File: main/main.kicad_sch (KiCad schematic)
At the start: 0 parts

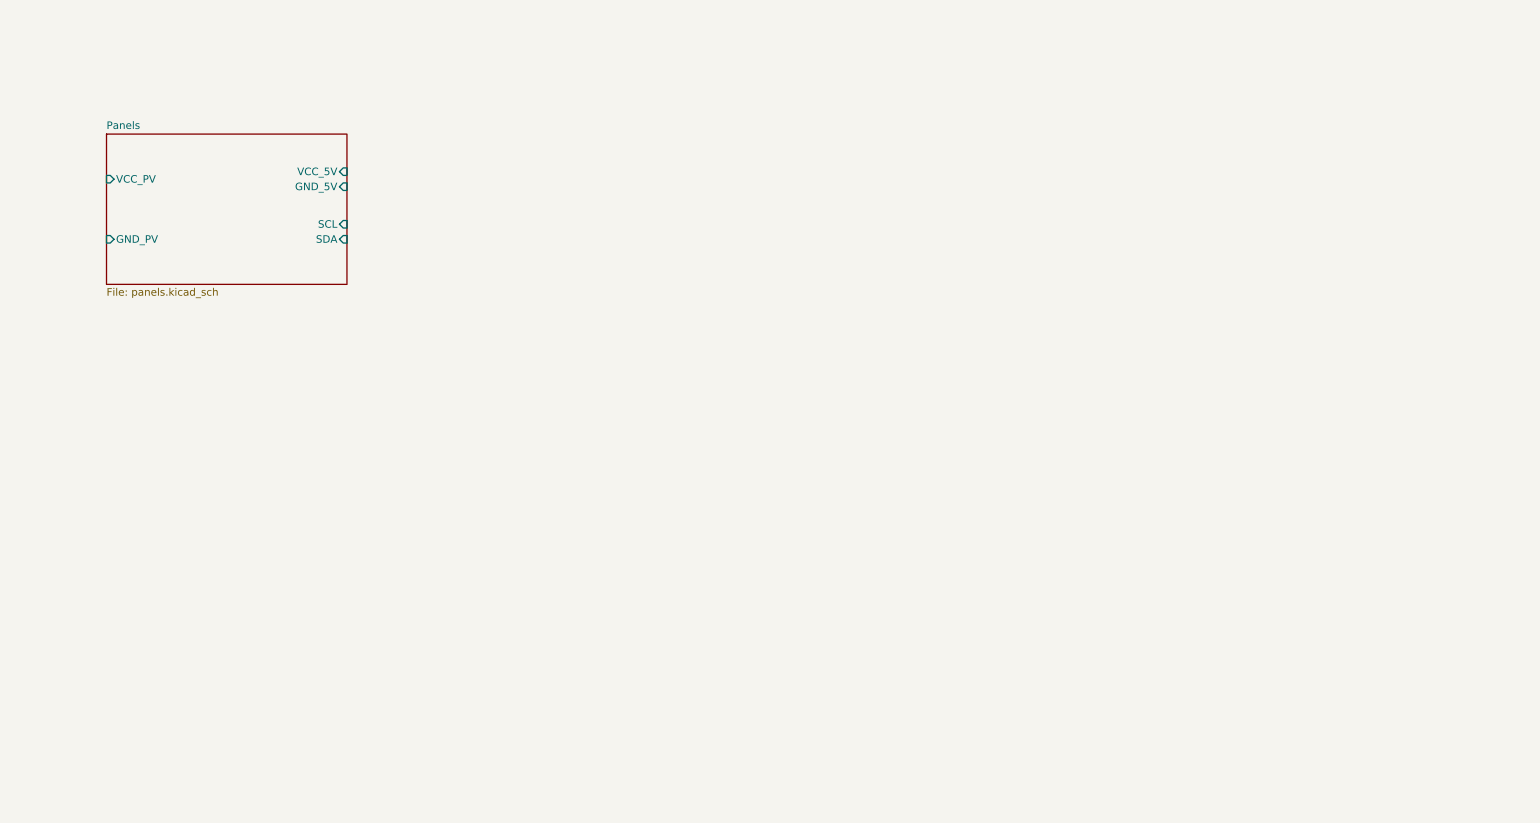
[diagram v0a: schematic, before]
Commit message: added MCU to PV
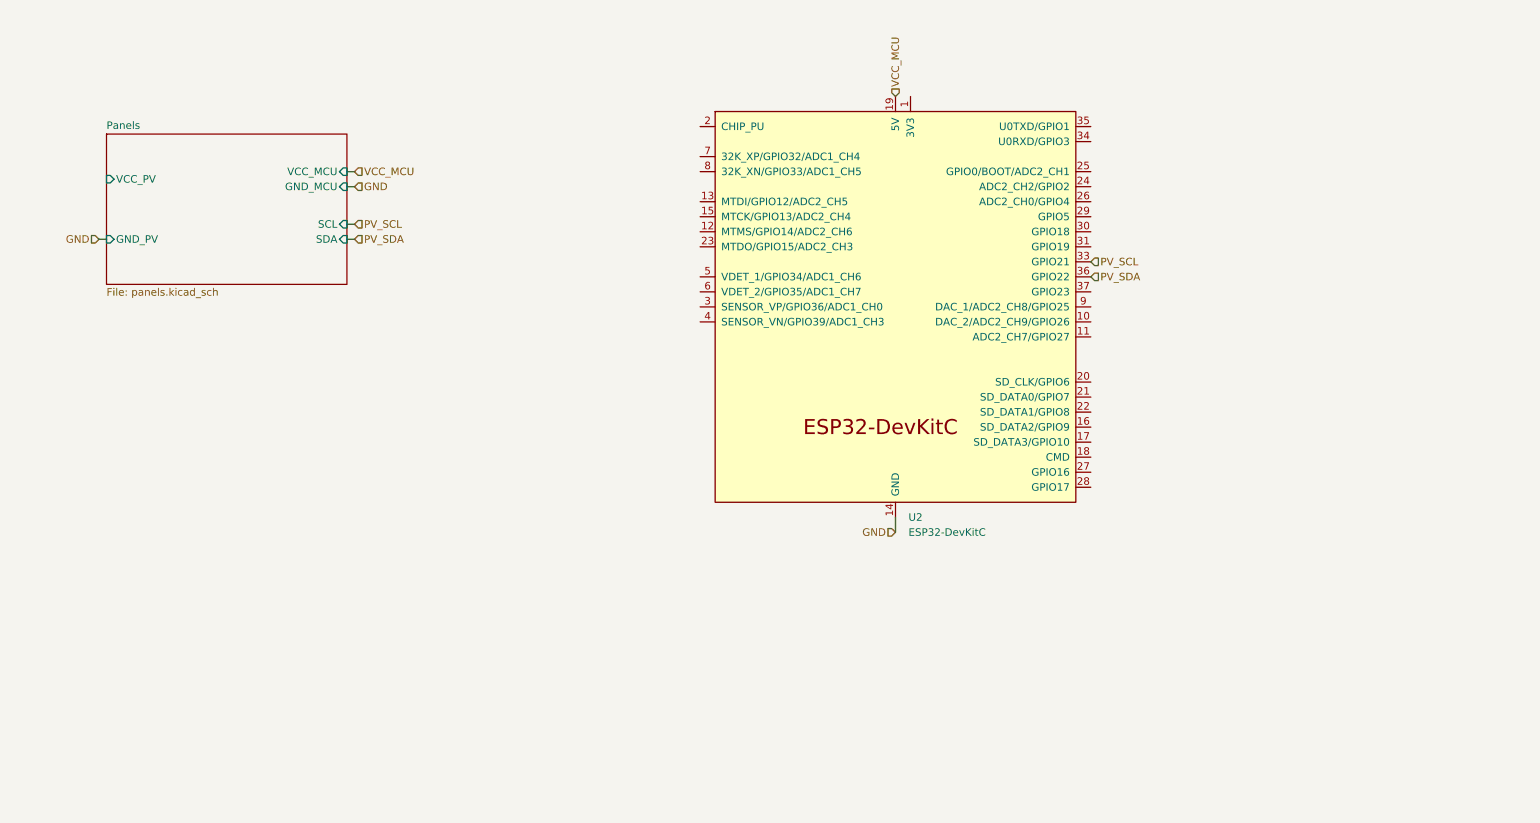
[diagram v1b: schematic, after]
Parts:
- added U2: ESP32-DevKitC, PCM_Espressif:ESP32-DevKitC, symbol PCM_Espressif:ESP32-DevKitC
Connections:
- new net GND: U2.14 (GND), U2.32 (GND), U2.38 (GND)
- new net PV_SCL: U2.33 (GPIO21)
- new net PV_SDA: U2.36 (GPIO22)
- new net VCC_MCU: U2.19 (5V)
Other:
- sheet Panels ports: added GND_MCU, VCC_MCU; removed GND_5V, VCC_5V

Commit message: added MPPT and Battery
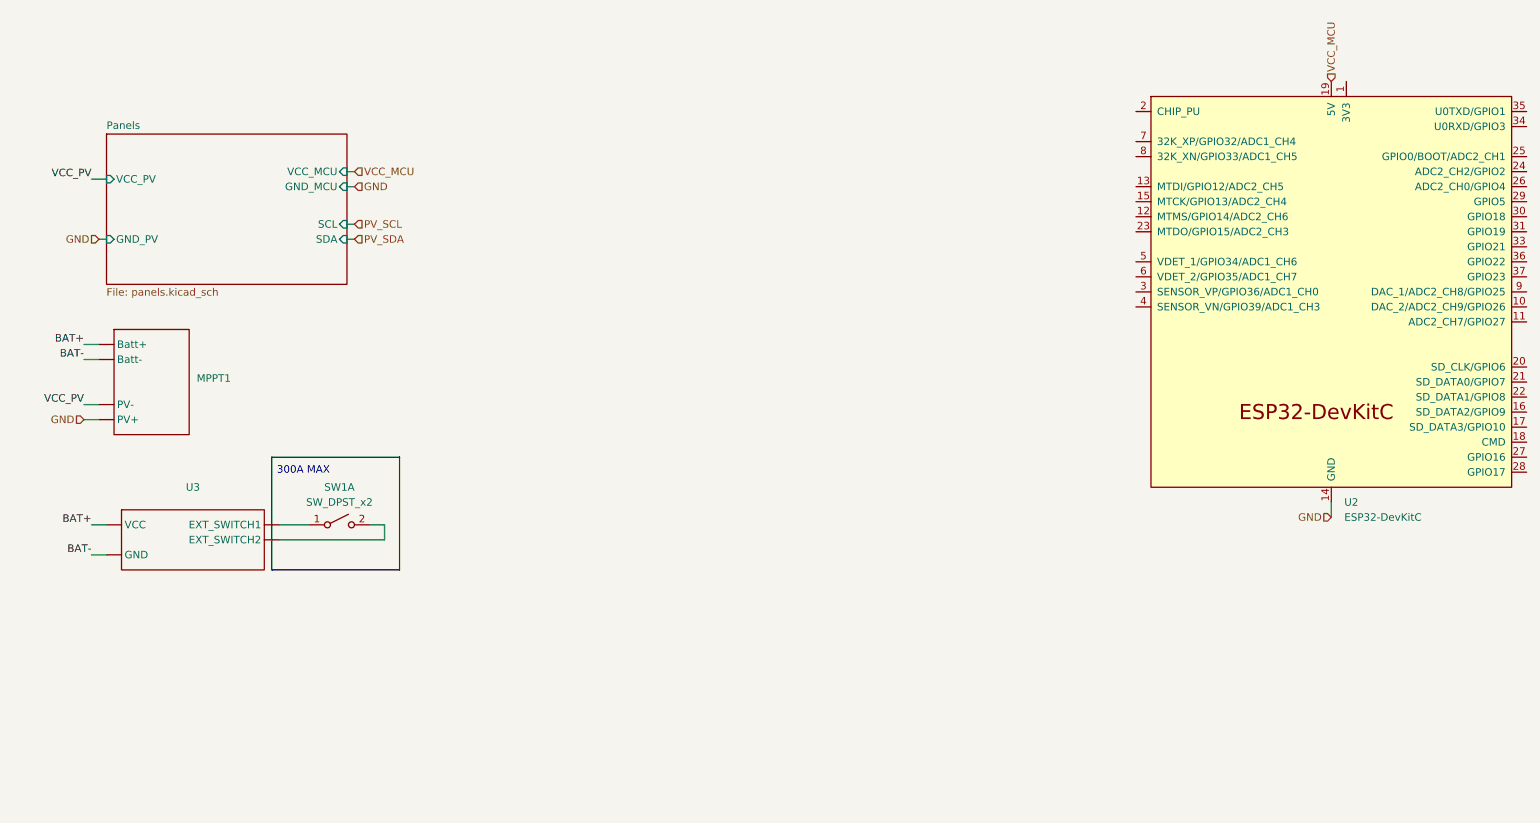
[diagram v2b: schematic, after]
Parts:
- added MPPT1: ~, symbol New_Library_0:MPPT_Victron_150{backslash}35
- added SW1: SW_DPST_x2, symbol Switch:SW_DPST_x2
- added U3: ~, symbol New_Library_0:Accumulator
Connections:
- net GND: now also MPPT1. (PV-)
- net PV_SCL: no longer U2.33 (GPIO21)
- net PV_SDA: no longer U2.36 (GPIO22)
- new net: SW1.1 (A), U3. (VCC)
- new net: SW1.2 (B), U3. (VCC)
- new net BAT+: MPPT1. (PV-), U3. (VCC)
- new net BAT-: MPPT1. (PV-), U3. (VCC)
- new net VCC_PV: MPPT1. (PV-)
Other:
- note added: "300A MAX"
- moved on the sheet: U2

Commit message: Added Central Control Unit Added Jetson Orin Nano
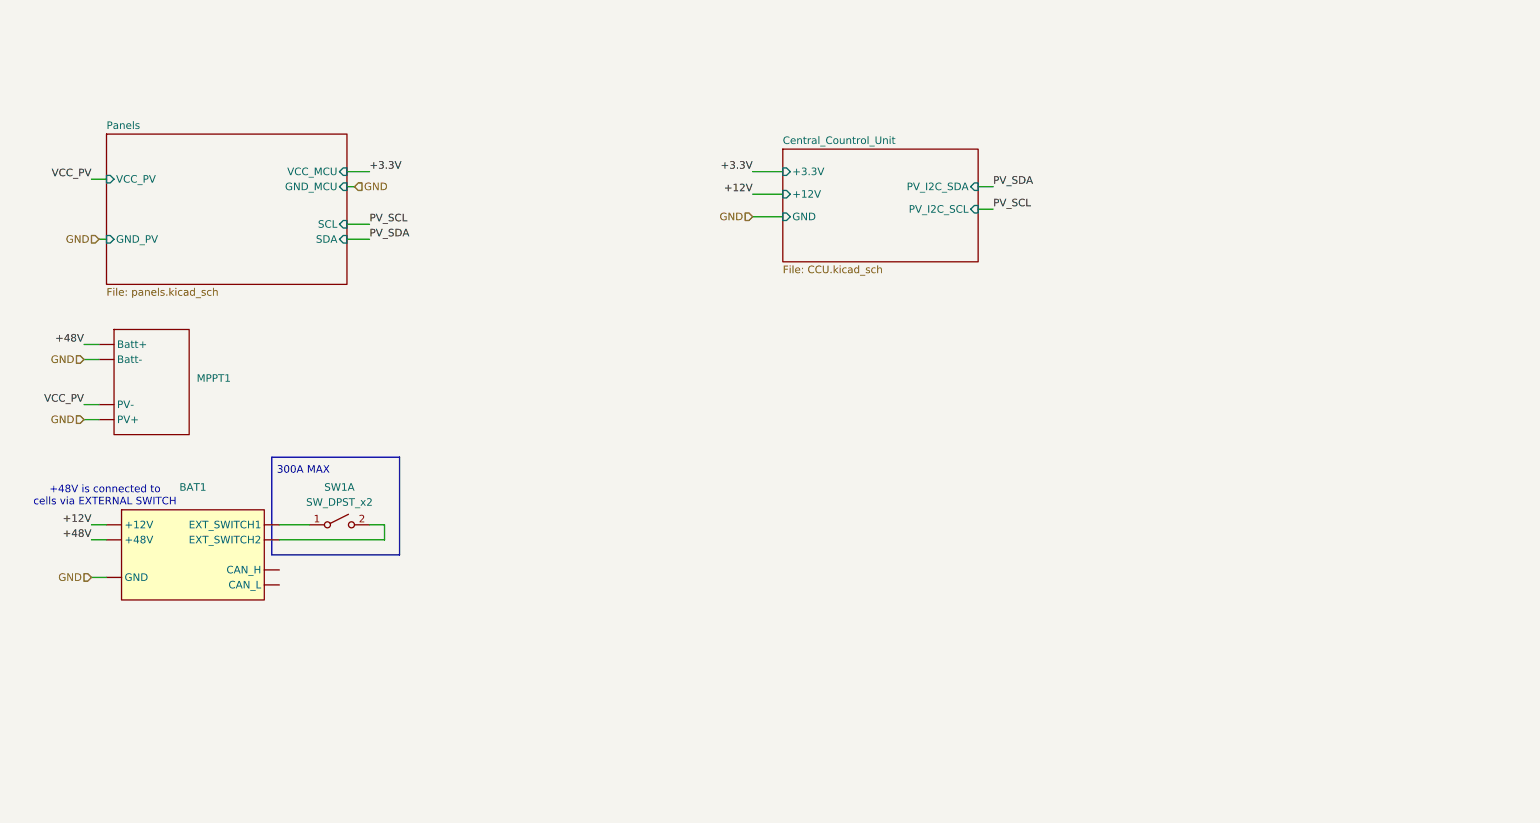
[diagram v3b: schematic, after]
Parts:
- removed U2: ESP32-DevKitC, PCM_Espressif:ESP32-DevKitC, symbol PCM_Espressif:ESP32-DevKitC
- renumbered U3 to BAT1
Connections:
- net GND: now also BAT1. (GND)
- removed net BAT+: BAT1. (VCC), MPPT1. (PV-)
- removed net BAT-: BAT1. (VCC), MPPT1. (PV-)
- new net +12V: BAT1. (GND)
- new net +48V: BAT1. (GND), MPPT1. (PV-)
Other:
- added sheet Central_Countrol_Unit (CCU.kicad_sch)
- note added: "+48V is connected to cells via EXTERNAL SWITCH"

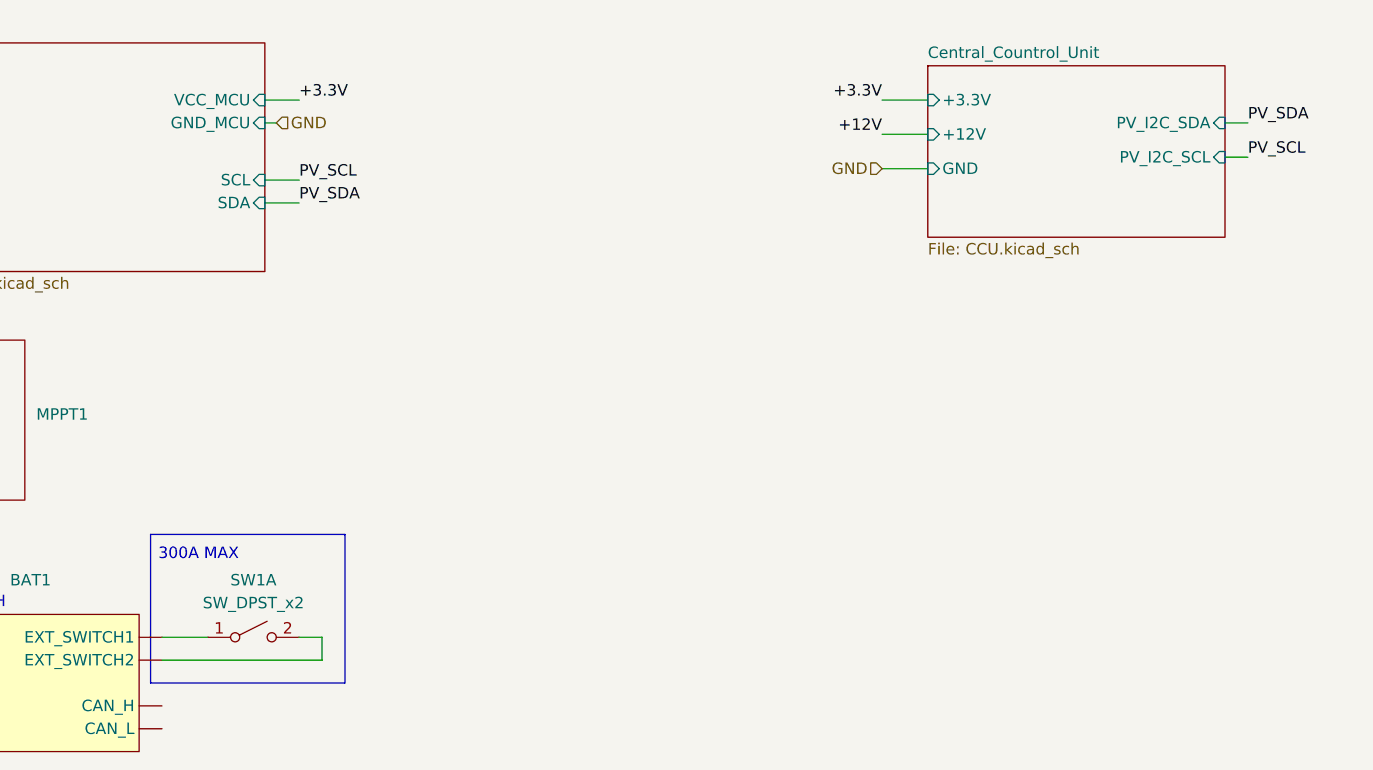
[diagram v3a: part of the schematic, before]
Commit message: Added CAN connection from BAT to CCU(Jetson)
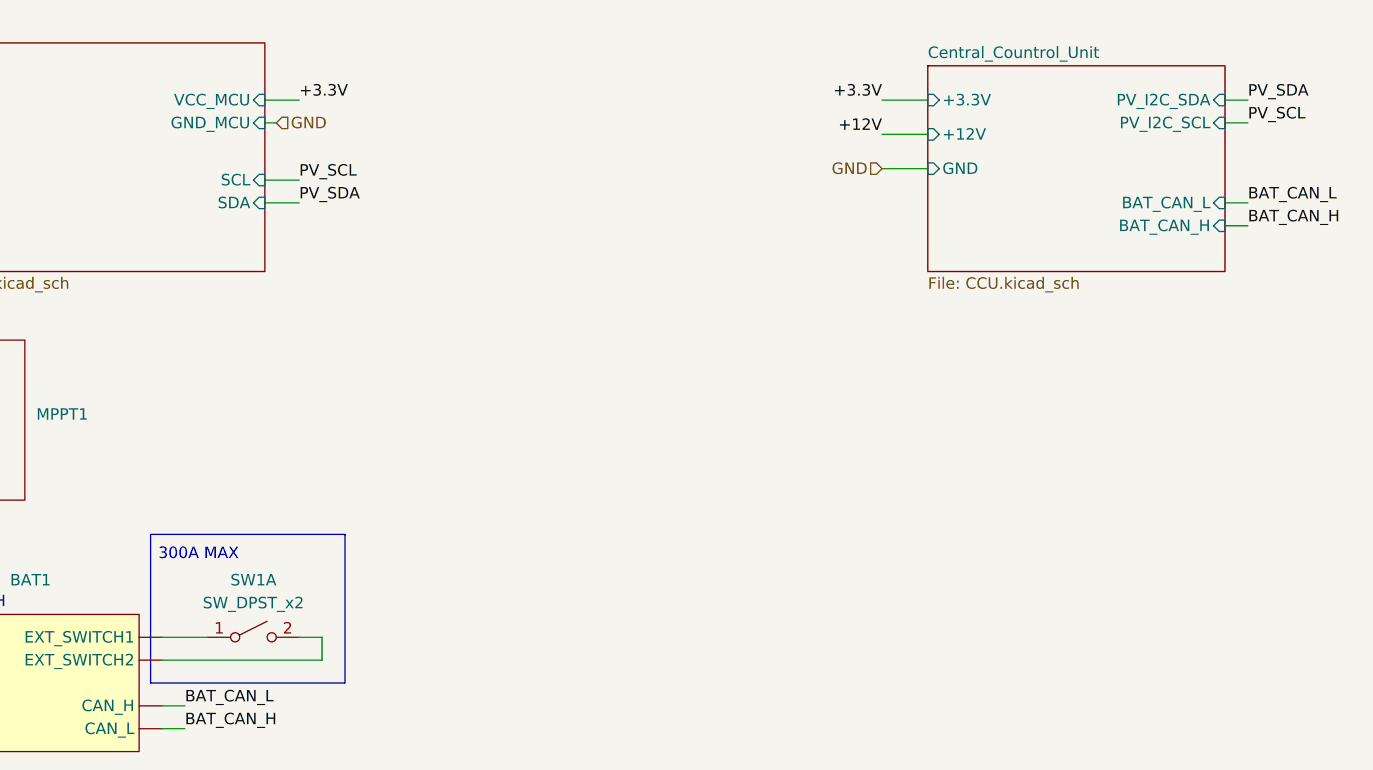
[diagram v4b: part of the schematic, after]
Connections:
- new net BAT_CAN_H: BAT1. (GND)
- new net BAT_CAN_L: BAT1. (GND)
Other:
- sheet Central_Countrol_Unit ports: added BAT_CAN_H, BAT_CAN_L; removed none
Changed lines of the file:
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@@
+	(wire
+		(pts
+			(xy 55.88 110.49) (xy 58.42 110.49)
+		)
+		(stroke
+			(width 0)
+			(type default)
+		)
+	)
 	(wire
 		(pts
@@
 	(wire
 		(pts
+			(xy 173.99 54.61) (xy 176.53 54.61)
+		)
+		(stroke
+			(width 0)
+			(type default)
+		)
+	)
+	(wire
+		(pts
 			(xy 22.86 69.85) (xy 25.4 69.85)
 		)
@@
 	(wire
 		(pts
+			(xy 55.88 107.95) (xy 58.42 107.95)
+		)
+		(stroke
+			(width 0)
+			(type default)
+		)
+	)
+	(wire
+		(pts
+			(xy 173.99 40.64) (xy 176.53 40.64)
+		)
+		(stroke
+			(width 0)
+			(type default)
+		)
+	)
+	(wire
+		(pts
+			(xy 73.66 100.33) (xy 73.66 102.87)
+		)
+		(stroke
+			(width 0)
+			(type default)
+		)
+	)
+	(wire
+		(pts
+			(xy 22.86 72.39) (xy 25.4 72.39)
+		)
+		(stroke
+			(width 0)
+			(type default)
+		)
+	)
+	(wire
+		(pts
+			(xy 22.86 82.55) (xy 25.4 82.55)
+		)
+		(stroke
+			(width 0)
+			(type default)
+		)
+	)
+	(wire
+		(pts
+			(xy 140.97 40.64) (xy 135.89 40.64)
+		)
+		(stroke
+			(width 0)
+			(type default)
+		)
+	)
+	(wire
+		(pts
+			(xy 24.13 41.91) (xy 26.67 41.91)
+		)
+		(stroke
+			(width 0)
+			(type default)
+		)
+	)
+	(wire
+		(pts
+			(xy 55.88 102.87) (xy 73.66 102.87)
+		)
+		(stroke
+			(width 0)
+			(type default)
+		)
+	)
+	(wire
+		(pts
+			(xy 24.13 102.87) (xy 26.67 102.87)
+		)
+		(stroke
+			(width 0)
+			(type default)
+		)
+	)
+	(wire
+		(pts
+			(xy 25.4 52.07) (xy 26.67 52.07)
+		)
+		(stroke
+			(width 0)
+			(type default)
+		)
+	)
+	(wire
+		(pts
+			(xy 67.31 40.64) (xy 71.12 40.64)
+		)
+		(stroke
+			(width 0)
+			(type default)
+		)
+	)
+	(wire
+		(pts
+			(xy 24.13 109.22) (xy 26.67 109.22)
+		)
+		(stroke
+			(width 0)
+			(type default)
+		)
+	)
+	(wire
+		(pts
+			(xy 135.89 44.45) (xy 140.97 44.45)
+		)
+		(stroke
+			(width 0)
+			(type default)
+		)
+	)
+	(wire
+		(pts
+			(xy 67.31 52.07) (xy 71.12 52.07)
+		)
+		(stroke
+			(width 0)
+			(type default)
+		)
+	)
+	(wire
+		(pts
 			(xy 173.99 43.18) (xy 176.53 43.18)
 		)
@@
 	(wire
 		(pts
-			(xy 73.66 100.33) (xy 73.66 102.87)
-		)
-		(stroke
-			(width 0)
-			(type default)
-		)
-	)
-	(wire
-		(pts
-			(xy 22.86 72.39) (xy 25.4 72.39)
-		)
-		(stroke
-			(width 0)
-			(type default)
-		)
-	)
-	(wire
-		(pts
-			(xy 22.86 82.55) (xy 25.4 82.55)
-		)
-		(stroke
-			(width 0)
-			(type default)
-		)
-	)
-	(wire
-		(pts
-			(xy 140.97 40.64) (xy 135.89 40.64)
-		)
-		(stroke
-			(width 0)
-			(type default)
-		)
-	)
-	(wire
-		(pts
-			(xy 24.13 41.91) (xy 26.67 41.91)
-		)
-		(stroke
-			(width 0)
-			(type default)
-		)
-	)
-	(wire
-		(pts
-			(xy 55.88 102.87) (xy 73.66 102.87)
-		)
-		(stroke
-			(width 0)
-			(type default)
-		)
-	)
-	(wire
-		(pts
-			(xy 24.13 102.87) (xy 26.67 102.87)
-		)
-		(stroke
-			(width 0)
-			(type default)
-		)
-	)
-	(wire
-		(pts
-			(xy 25.4 52.07) (xy 26.67 52.07)
-		)
-		(stroke
-			(width 0)
-			(type default)
-		)
-	)
-	(wire
-		(pts
-			(xy 67.31 40.64) (xy 71.12 40.64)
-		)
-		(stroke
-			(width 0)
-			(type default)
-		)
-	)
-	(wire
-		(pts
-			(xy 24.13 109.22) (xy 26.67 109.22)
-		)
-		(stroke
-			(width 0)
-			(type default)
-		)
-	)
-	(wire
-		(pts
-			(xy 135.89 44.45) (xy 140.97 44.45)
-		)
-		(stroke
-			(width 0)
-			(type default)
-		)
-	)
-	(wire
-		(pts
-			(xy 67.31 52.07) (xy 71.12 52.07)
-		)
-		(stroke
-			(width 0)
-			(type default)
-		)
-	)
-	(wire
-		(pts
-			(xy 173.99 46.99) (xy 176.53 46.99)
+			(xy 173.99 52.07) (xy 176.53 52.07)
 		)
 		(stroke
@@
 		)
 	)
+	(label "BAT_CAN_H"
+		(at 176.53 54.61 0)
+		(fields_autoplaced yes)
+		(effects
+			(font
+				(size 1.27 1.27)
+			)
+			(justify left bottom)
+		)
+	)
 	(label "+12V"
 		(at 24.13 100.33 180)
@@
 	)
 	(label "PV_SDA"
-		(at 176.53 43.18 0)
+		(at 176.53 40.64 0)
 		(fields_autoplaced yes)
 		(effects
@@
 		)
 	)
+	(label "BAT_CAN_L"
+		(at 176.53 52.07 0)
+		(fields_autoplaced yes)
+		(effects
+			(font
+				(size 1.27 1.27)
+			)
+			(justify left bottom)
+		)
+	)
 	(label "VCC_PV"
 		(at 22.86 80.01 180)
@@
 	)
 	(label "PV_SCL"
-		(at 176.53 46.99 0)
+		(at 176.53 43.18 0)
+		(fields_autoplaced yes)
+		(effects
+			(font
+				(size 1.27 1.27)
+			)
+			(justify left bottom)
+		)
+	)
+	(label "BAT_CAN_H"
+		(at 58.42 110.49 0)
+		(fields_autoplaced yes)
+		(effects
+			(font
+				(size 1.27 1.27)
+			)
+			(justify left bottom)
+		)
+	)
+	(label "BAT_CAN_L"
+		(at 58.42 107.95 0)
 		(fields_autoplaced yes)
 		(effects
@@
 	(sheet
 		(at 140.97 36.83)
-		(size 33.02 19.05)
+		(size 33.02 22.86)
 		(fields_autoplaced yes)
 		(stroke
@@
 		)
 		(property "Sheetfile" "CCU.kicad_sch"
-			(at 140.97 56.4646 0)
+			(at 140.97 60.2746 0)
 			(effects
 				(font
@@
 		)
 		(pin "PV_I2C_SDA" input
+			(at 173.99 40.64 0)
+			(effects
+				(font
+					(size 1.27 1.27)
+				)
+				(justify right)
+			)
+		)
+		(pin "PV_I2C_SCL" input
 			(at 173.99 43.18 0)
-			(effects
-				(font
-					(size 1.27 1.27)
-				)
-				(justify right)
-			)
-		)
-		(pin "PV_I2C_SCL" input
-			(at 173.99 46.99 0)
 			(effects
 				(font
@@
 			)
 		)
+		(pin "BAT_CAN_L" input
+			(at 173.99 52.07 0)
+			(effects
+				(font
+					(size 1.27 1.27)
+				)
+				(justify right)
+			)
+		)
+		(pin "BAT_CAN_H" input
+			(at 173.99 54.61 0)
+			(effects
+				(font
+					(size 1.27 1.27)
+				)
+				(justify right)
+			)
+		)
